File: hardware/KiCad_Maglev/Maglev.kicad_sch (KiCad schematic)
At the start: 24 parts, among them J1 USB_C_Receptacle, J11 61300421121, J4 694106301002, J6 61300621121, J8 61300421121, U1 ESP32-C3, U3 WE-TVS-82400102

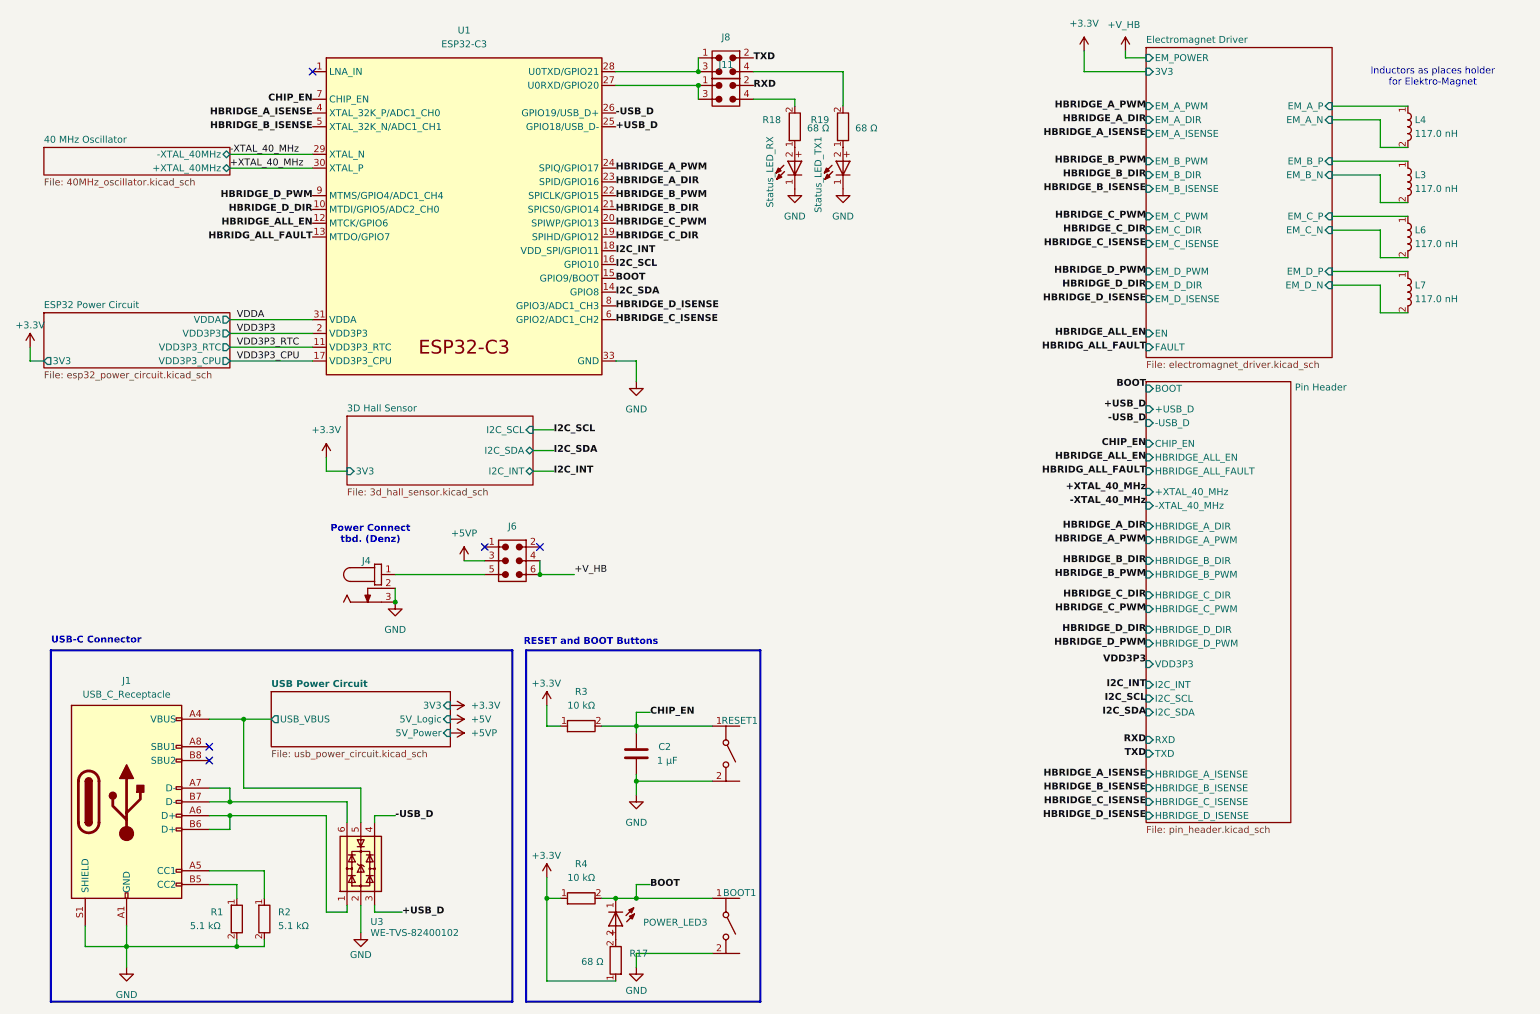
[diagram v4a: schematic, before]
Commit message: Added Footprints/Models for coil and ringmagnet, changed most components to 1206 series
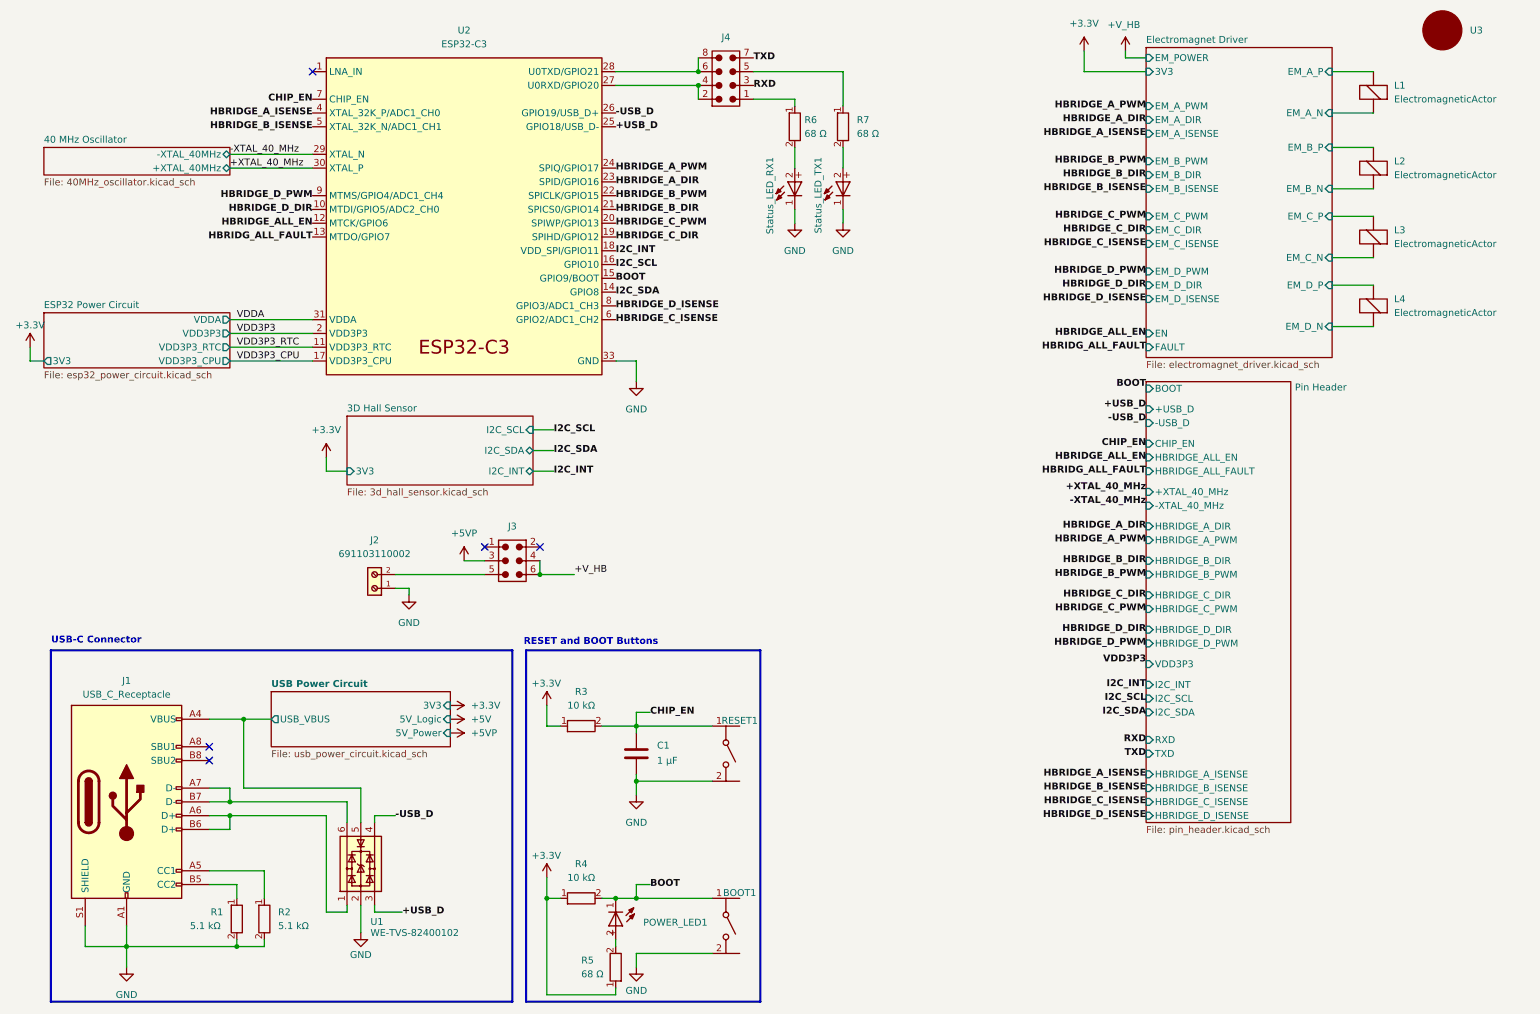
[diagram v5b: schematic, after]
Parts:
- removed C2: 0805_H1.25_R_885012107015, Capacitor_SMD_Wurth:C_Wurth_WCAP-CSGP-0805_H1.25_R, symbol Capacitor_Wurth_WCAP-CSGP:0805_H1.25_R_885012107015
- removed J11, J8: 61300421121, Connector_THT_Wurth:J_Wurth_WR-PHD_61300421121, symbol Connector_Wurth_WR-PHD:61300421121
- removed J4: 694106301002, Connector_THT_Wurth:J_Wurth_WR-DC_694106301002, symbol Connector_Wurth_WR-DC:694106301002
- removed L3, L4, L6, L7: 1212_7449152111, Inductor_SMD_Wurth:L_Wurth_WE-ACHC-1212_7449152111, symbol Inductor_Wurth_WE-ACHC:1212_7449152111
- removed R17, R18, R19: 1206_R_560112132050, Resistor_SMD_Wurth:R_Wurth_WRIS-RSKS-1206_R, symbol Resistor_Wurth_WRIS-RSKS:1206_R_560112132050
- removed R3, R4: 0402_560112110020, Resistor_SMD_Wurth:R_Wurth_WRIS-RSKS-0402, symbol Resistor_Wurth_WRIS-RSKS:0402_560112110020
- added C1: 1206_H1.6_885012208093, Capacitor_SMD_Wurth:C_Wurth_WCAP-CSGP-1206_H1.6, symbol Capacitor_Wurth_WCAP-CSGP:1206_H1.6_885012208093
- added J2: 691103110002, 691103110002:691103110002, symbol 691103110002:691103110002
- added J4: 61300821121, Connector_THT_Wurth:J_Wurth_WR-PHD_61300821121, symbol Connector_Wurth_WR-PHD:61300821121
- added L1, L2, L3, L4: ElectromagneticActor, CUSTOM:EM, symbol Device:ElectromagneticActor
- added R3, R4: 1206_R_560112132018, Resistor_SMD_Wurth:R_Wurth_WRIS-RSKS-1206_R, symbol Resistor_Wurth_WRIS-RSKS:1206_R_560112132018
- added R5, R6, R7: 1206_R_560112132050, Resistor_SMD_Wurth:R_Wurth_WRIS-RSKS-1206_R, symbol Resistor_Wurth_WRIS-RSKS:1206_R_560112132050
- added U3: (no value), CUSTOM:MagnetRing, symbol CUSTOM:MagnetRing
- renumbered J6 to J3, POWER_LED3 to POWER_LED1, Status_LED_RX to Status_LED_RX1, U3 to U1, U1 to U2
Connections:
- net +3.3V: now also R3.1, R4.1, R5.1
- net BOOT: now also R4.2
- net CHIP_EN: now also C1.1, R3.2
- net Electromagnet Driver/EM_A_N: now also L1.1 (-)
- net Electromagnet Driver/EM_A_P: now also L1.2 (+)
- net Electromagnet Driver/EM_B_N: now also L2.1 (-)
- net Electromagnet Driver/EM_B_P: now also L2.2 (+)
- net Electromagnet Driver/EM_C_N: now also L3.1 (-)
- net Electromagnet Driver/EM_C_P: now also L3.2 (+)
- net Electromagnet Driver/EM_D_N: now also L4.1 (-)
- net Electromagnet Driver/EM_D_P: now also L4.2 (+)
- net GND: now also C1.2, J2.1
- net RXD: now also J4.3
- net TXD: now also J4.7
- net at POWER_LED1.2 (+): now also R5.2
- net at U2.27 (U0RXD/GPIO20): now also J4.2, J4.4
- net at U2.28 (U0TXD/GPIO21): now also J4.6, J4.8
- net at J3.5: now also J2.2
- net at Status_LED_RX1.2 (+): now also R6.2
- net at Status_LED_TX1.2 (+): now also R7.2
- new net: J4.1, R6.1
- new net: J4.5, R7.1
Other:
- note removed: "Inductors as places holder for Elektro-Magnet"
- note removed: "Power Connect tbd. (Denz)"
- moved on the sheet: Status_LED_RX1, Status_LED_TX1

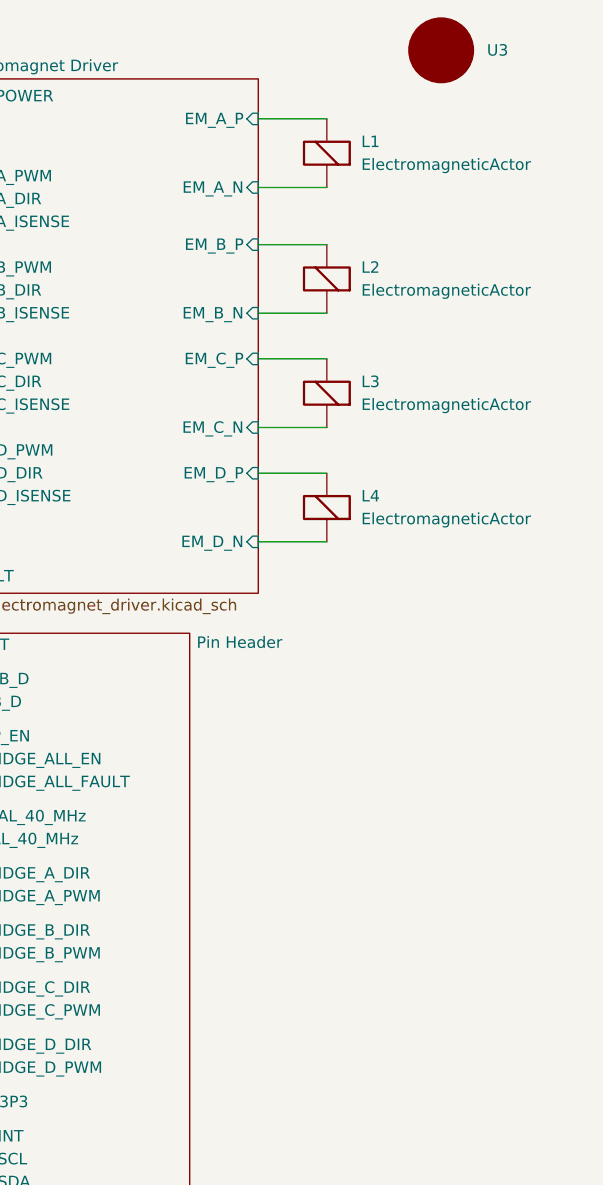
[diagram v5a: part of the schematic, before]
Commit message: Spacer Footprints added, updated some libraries
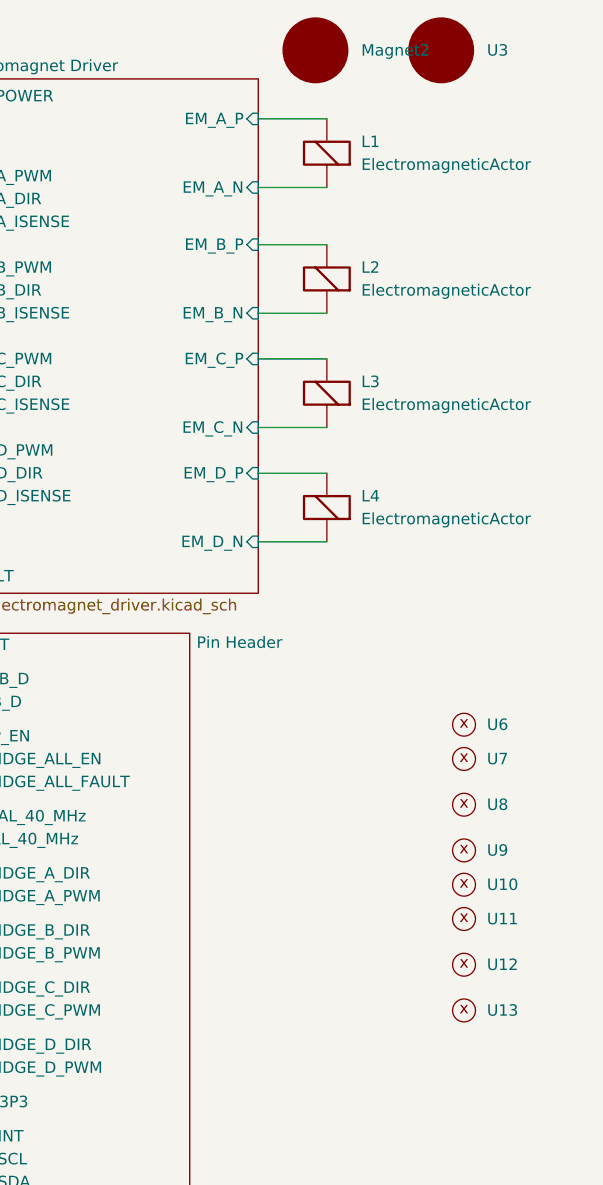
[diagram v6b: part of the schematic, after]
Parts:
- added Magnet2: (no value), CUSTOM:MagnetRing_2, symbol CUSTOM:MagnetRing
- added U10, U11, U12, U13, U6, U7, U8, U9: (no value), CUSTOM:Spacer, symbol CUSTOM:Spacer

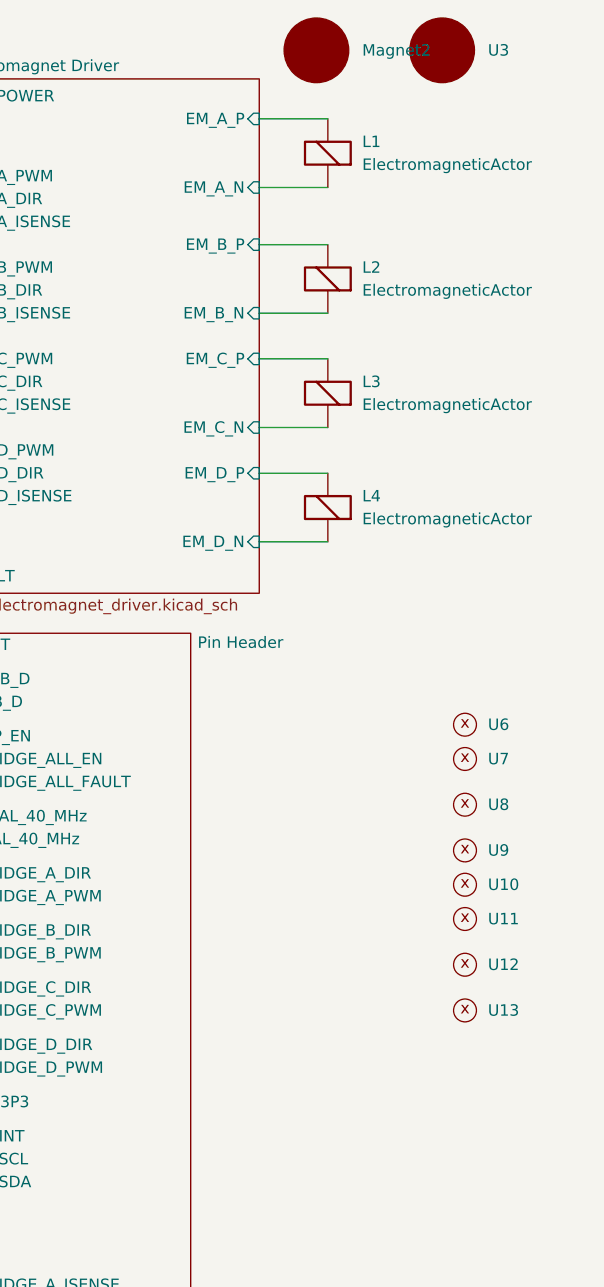
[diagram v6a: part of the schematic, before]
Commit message: changed mounting and spacing system and  some detail changes
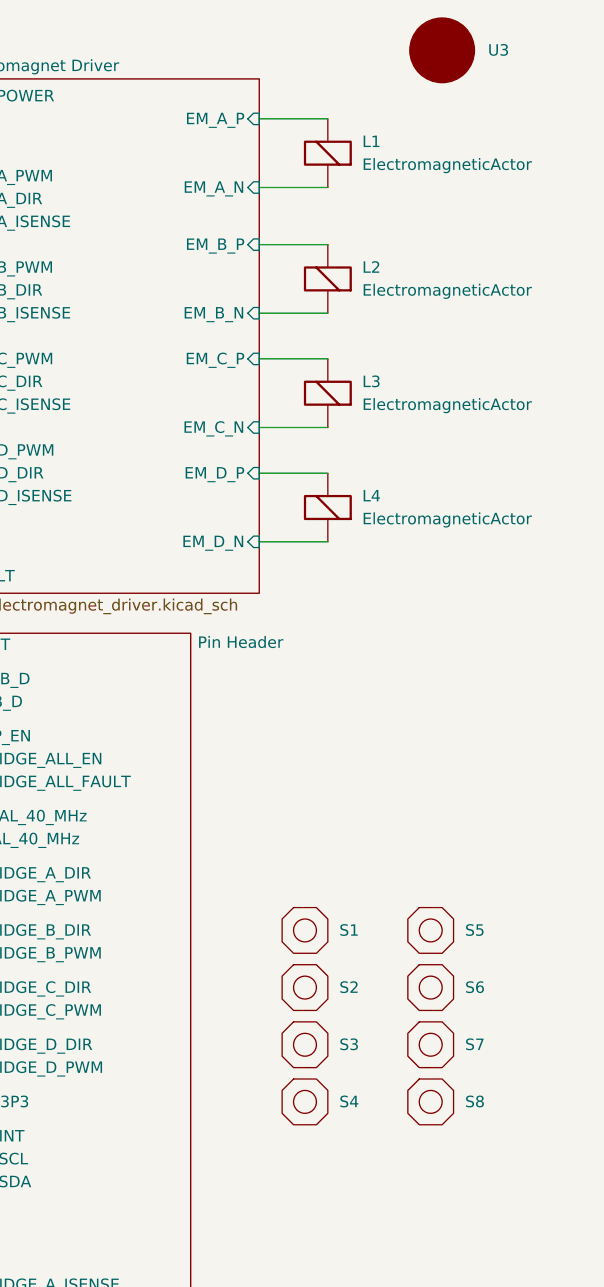
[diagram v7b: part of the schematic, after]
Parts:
- removed Magnet2: (no value), CUSTOM:MagnetRing_2, symbol CUSTOM:MagnetRing
- removed U10, U11, U12, U13, U6, U7, U8, U9: (no value), CUSTOM:Spacer, symbol CUSTOM:Spacer
- added S1, S2, S3, S4: (no value), CUSTOM:Spacer_15mm, symbol CUSTOM:Spacer
- added S5, S6, S7, S8: (no value), CUSTOM:Spacer_20mm, symbol CUSTOM:Spacer
- L1, L2, L3, L4: footprint CUSTOM:EM -> CUSTOM:Electromagnet
